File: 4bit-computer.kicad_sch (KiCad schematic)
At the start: 0 parts

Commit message: new plaque
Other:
- company: ELIT -> Abteilung ELIT
- title: 4bit Computer -> 4bit Ripple Carry Adder
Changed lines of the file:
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@@
 	(paper "A4")
 	(title_block
-		(title "4bit Computer")
+		(title "4bit Ripple Carry Adder")
 		(date "2026-09-29")
 		(rev "V1.0 / R1")
-		(company "ELIT")
-		(comment 1 "AndF BinJ ObeM SinS")
+		(company "Abteilung ELIT")
+		(comment 1 "AndF JunJ ObeM SinS")
 		(comment 2 "3AHELS")
 		(comment 3 "AndF")
-		(comment 4 "AndF")
+		(comment 4 "SalH")
 		(comment 5 "HauP")
 		(comment 6 "Schematic")

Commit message: renamed ALU + exported pdf
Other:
- sheet ripple-carry-adder renamed Arithmetic Logic Unit
- sheet Arithmetic Logic Unit: file ripple-carry-adder.kicad_sch -> alu.kicad_sch
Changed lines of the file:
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@@
 			(color 0 0 0 0)
 		)
-		(property "Sheetname" "ripple-carry-adder"
+		(property "Sheetname" "Arithmetic Logic Unit"
 			(at 203.2 37.3884 0)
 			(show_name no)
@@
 			)
 		)
-		(property "Sheetfile" "ripple-carry-adder.kicad_sch"
+		(property "Sheetfile" "alu.kicad_sch"
 			(at 203.2 64.0846 0)
 			(show_name no)

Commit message: renamed files
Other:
- title: 4bit Ripple Carry Adder -> Arithmetic Logic Unit
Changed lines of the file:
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@@
 	(paper "A4")
 	(title_block
-		(title "4bit Ripple Carry Adder")
+		(title "Arithmetic Logic Unit")
 		(date "2026-09-29")
 		(rev "V1.0 / R1")

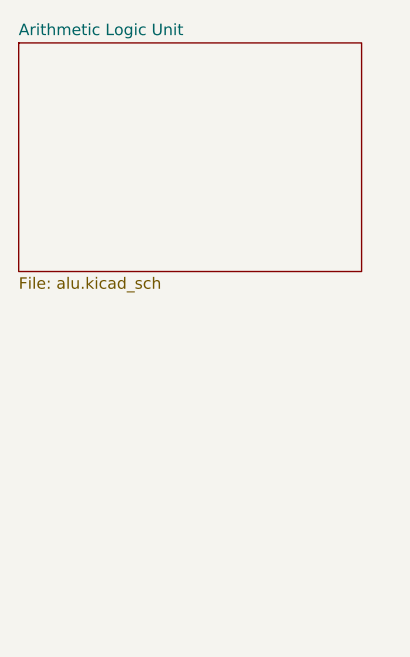
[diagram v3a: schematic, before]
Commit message: added 4bit-program counter in KiCAD
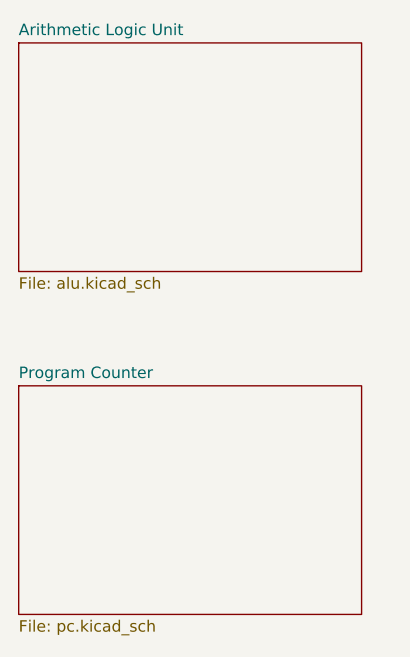
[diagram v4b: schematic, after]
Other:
- added sheet Program Counter (pc.kicad_sch)
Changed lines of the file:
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@@
+		)
+	)
+	(sheet
+		(at 203.2 76.2)
+		(size 38.1 25.4)
+		(exclude_from_sim no)
+		(in_bom yes)
+		(on_board yes)
+		(dnp no)
+		(fields_autoplaced yes)
+		(stroke
+			(width 0.1524)
+			(type solid)
+		)
+		(fill
+			(color 0 0 0 0)
+		)
+		(property "Sheetname" "Program Counter"
+			(at 203.2 75.4884 0)
+			(show_name no)
+			(do_not_autoplace no)
+			(effects
+				(font
+					(size 1.27 1.27)
+				)
+				(justify left bottom)
+			)
+		)
+		(property "Sheetfile" "pc.kicad_sch"
+			(at 203.2 102.1846 0)
+			(show_name no)
+			(do_not_autoplace no)
+			(effects
+				(font
+					(size 1.27 1.27)
+				)
+				(justify left top)
+			)
+		)
+		(instances
+			(project "4bit-computer"
+				(path "/1a564276-6752-45b4-a33a-f4bcbe787514"
+					(page "3")
+				)
+			)
 		)
 	)

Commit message: addes pc sim + kicad fix
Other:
- title: Arithmetic Logic Unit -> 4bit Computer
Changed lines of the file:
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@@
 	(paper "A4")
 	(title_block
-		(title "Arithmetic Logic Unit")
+		(title "4bit Computer")
 		(date "2026-09-29")
 		(rev "V1.0 / R1")
